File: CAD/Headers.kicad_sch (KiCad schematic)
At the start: 58 parts, among them J1 SWD, J10 OUT_0, J11 OUT_1, J12 OUT_2, J13 TEMP_0, J14 TEMP_1, J15 TEMP_2, J16 EXPANSION, J17 ESP_DB, J18 250-502/000-006, J19 A2543WV-5P, J2 A2543WV-2P, J20 IO_1, J21 IO_2, J22 A2543WV-2P, J23 CAN_1_OUT, J24 DRIVER_2, J25 DRIVER_1, J26 DRIVER_0, J28 SPI_DB, J3 OUT_6, J31 IO_3, J33 A2543WV-4P, J34 A2543WV-4P, J35 DRIVER_3, J36 DRIVER_4, J37 DRIVER_5, J38 CAN_0_OUT, J39 PANELDUE_SD, J4 OUT_7, J41 TEMP_3, J42 DS_LED, J44 IO_7_ISO_OUT, J47 IO_8_ISO_OUT, J48 SBC, J5 OUT_8, J50 EXT_5V_IN, J51 IO_4, J53 IO_5, J54 IO_6, J55 IO_7, J56 IO_8, J59 A2543WV-2P, J6 OUT_3, J60 A2543WV-2P, J61 IO_7_ISO_IN, J62 IO_8_ISO_IN, J7 OUT_4, J8 OUT_5

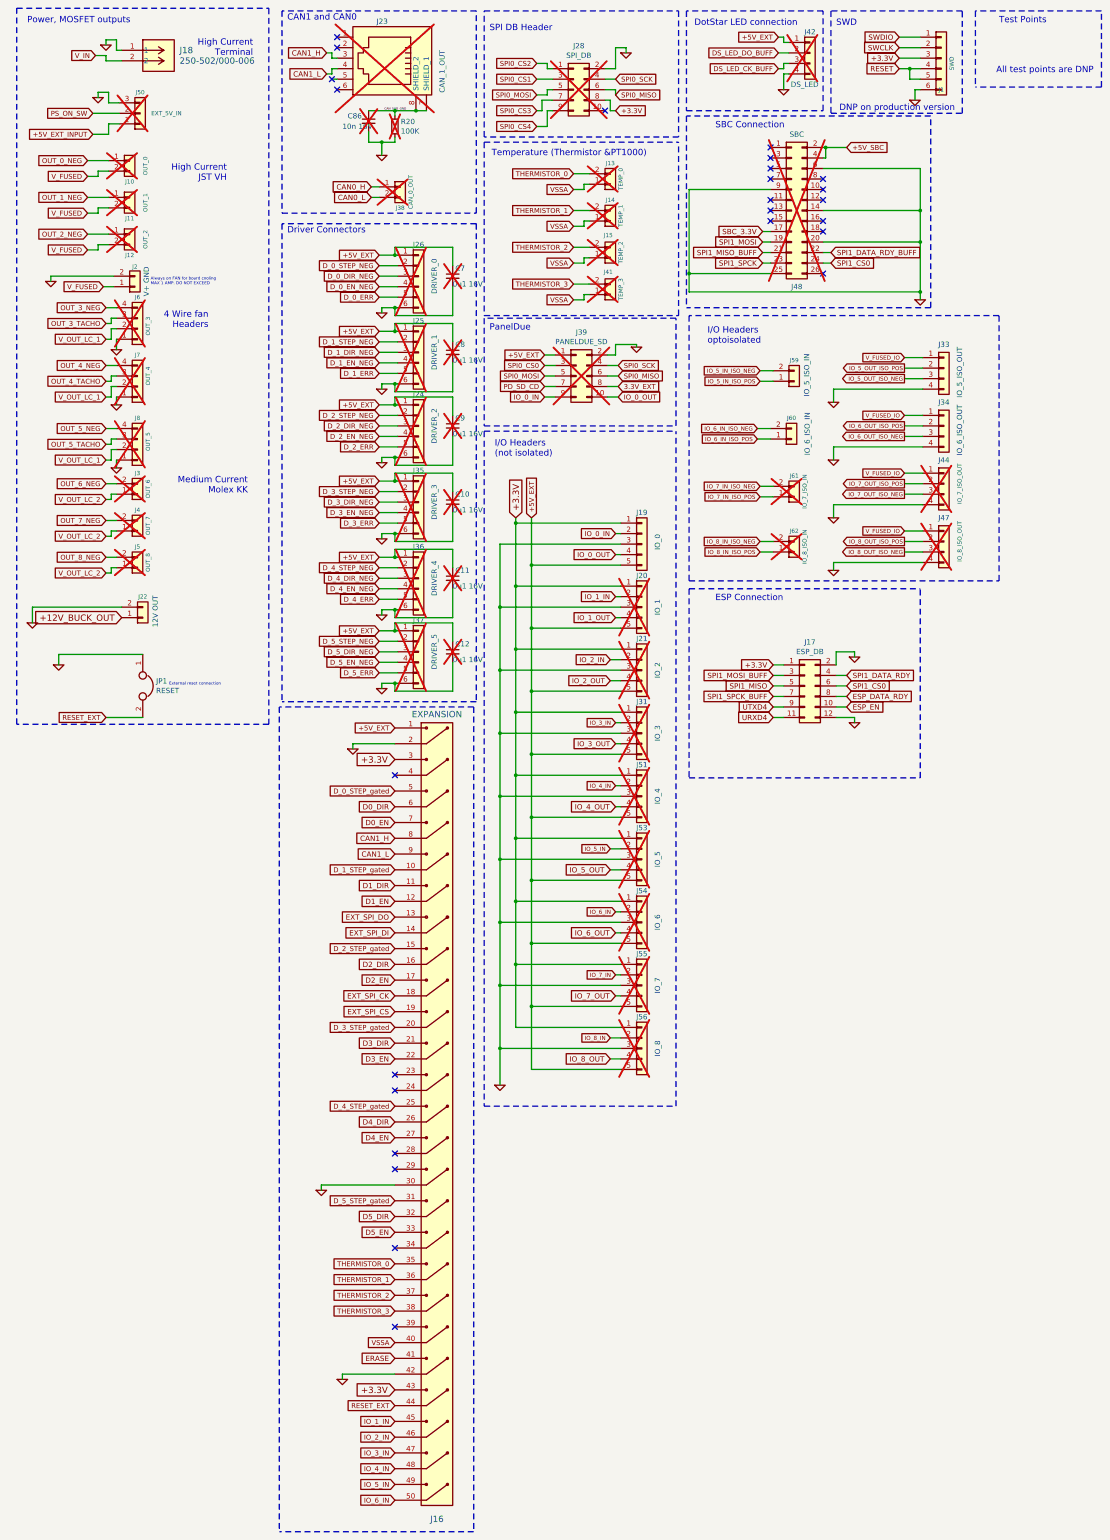
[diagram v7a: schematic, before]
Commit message: Remove Connectors
Removed all old and unused connectors outright from the schematic
Added several other connectors to DNP and Exclude BOM for production since those connectors have never been used.
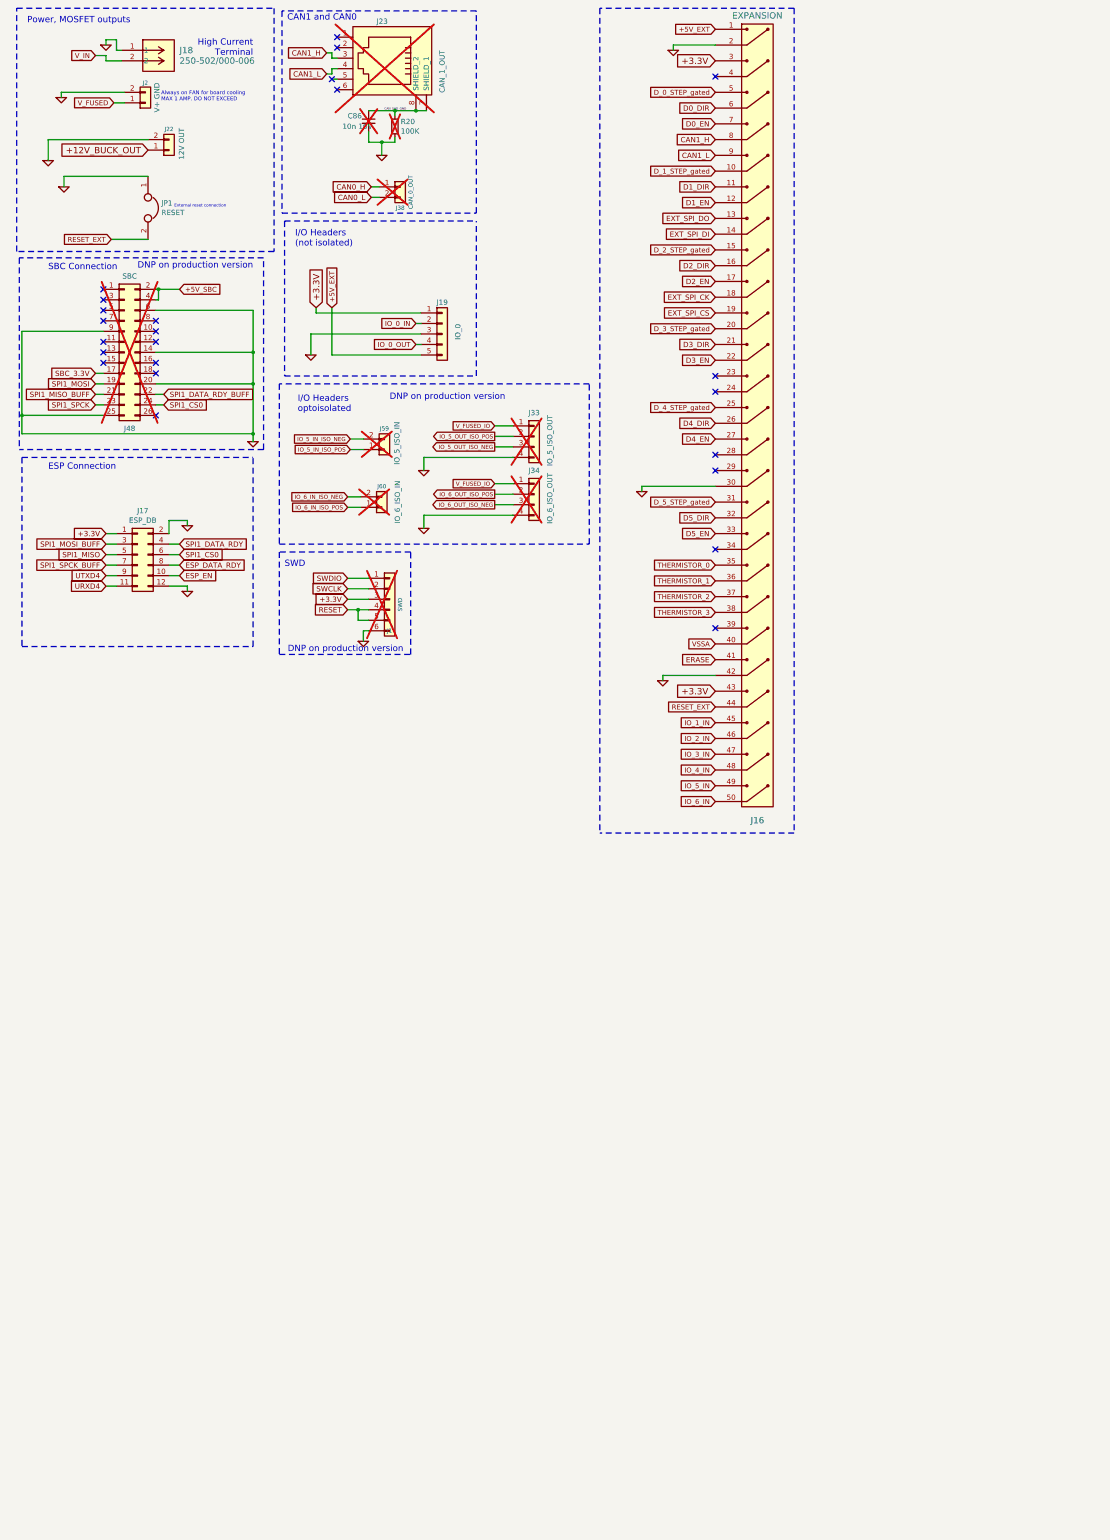
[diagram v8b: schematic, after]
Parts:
- removed C10, C11, C12, C7, C8, C9: 0u1 16V, Capacitor_SMD:C_0402_1005Metric_Wbry, symbol Device:C_Small
- removed J10: OUT_0, Connector_JST:JST_VH_B2P-VH-B_1x02_P3.96mm_Vertical, symbol Connector_Generic:Conn_01x02
- removed J11: OUT_1, Connector_JST:JST_VH_B2P-VH-B_1x02_P3.96mm_Vertical, symbol Connector_Generic:Conn_01x02
- removed J12: OUT_2, Connector_JST:JST_VH_B2P-VH-B_1x02_P3.96mm_Vertical, symbol Connector_Generic:Conn_01x02
- removed J13: TEMP_0, Connector_Molex:Wurth_61900211121-1x02_P2.54mm_Vertical-(Molex_KK-254_AE-6410-02Acompatible), symbol Connector_Generic:Conn_01x02
- removed J14: TEMP_1, Connector_Molex:Wurth_61900211121-1x02_P2.54mm_Vertical-(Molex_KK-254_AE-6410-02Acompatible), symbol Connector_Generic:Conn_01x02
- removed J15: TEMP_2, Connector_Molex:Wurth_61900211121-1x02_P2.54mm_Vertical-(Molex_KK-254_AE-6410-02Acompatible), symbol Connector_Generic:Conn_01x02
- removed J20: IO_1, Connector_Molex:Wurth_61900511121-1x05_P2.54mm_Vertical(Molex_KK-254_AE-6410-05A_Compatibe), symbol Connector_Generic:Conn_01x05
- removed J21: IO_2, Connector_Molex:Wurth_61900511121-1x05_P2.54mm_Vertical(Molex_KK-254_AE-6410-05A_Compatibe), symbol Connector_Generic:Conn_01x05
- removed J24: DRIVER_2, Connector_Molex:Wurth_61900611121-1x06_P2.54mm_Vertical(Molex_KK-254_AE-6410-06A_Compatibe), symbol Connector_Generic:Conn_01x06
- removed J25: DRIVER_1, Connector_Molex:Wurth_61900611121-1x06_P2.54mm_Vertical(Molex_KK-254_AE-6410-06A_Compatibe), symbol Connector_Generic:Conn_01x06
- removed J26: DRIVER_0, Connector_Molex:Wurth_61900611121-1x06_P2.54mm_Vertical(Molex_KK-254_AE-6410-06A_Compatibe), symbol Connector_Generic:Conn_01x06
- removed J28: SPI_DB, complib:MAX_TEMP_DB, symbol Connector_Generic:Conn_02x05_Odd_Even
- removed J3: OUT_6, Connector_Molex:Wurth_61900211121-1x02_P2.54mm_Vertical-(Molex_KK-254_AE-6410-02Acompatible), symbol Connector_Generic:Conn_01x02
- removed J31: IO_3, Connector_Molex:Wurth_61900511121-1x05_P2.54mm_Vertical(Molex_KK-254_AE-6410-05A_Compatibe), symbol Connector_Generic:Conn_01x05
- removed J35: DRIVER_3, Connector_Molex:Wurth_61900611121-1x06_P2.54mm_Vertical(Molex_KK-254_AE-6410-06A_Compatibe), symbol Connector_Generic:Conn_01x06
- removed J36: DRIVER_4, Connector_Molex:Wurth_61900611121-1x06_P2.54mm_Vertical(Molex_KK-254_AE-6410-06A_Compatibe), symbol Connector_Generic:Conn_01x06
- removed J37: DRIVER_5, Connector_Molex:Wurth_61900611121-1x06_P2.54mm_Vertical(Molex_KK-254_AE-6410-06A_Compatibe), symbol Connector_Generic:Conn_01x06
- removed J39: PANELDUE_SD, Connector_IDC:IDC-Header_2x05_P2.54mm_Vertical, symbol Connector_Generic:Conn_02x05_Odd_Even
- removed J4: OUT_7, Connector_Molex:Wurth_61900211121-1x02_P2.54mm_Vertical-(Molex_KK-254_AE-6410-02Acompatible), symbol Connector_Generic:Conn_01x02
- removed J41: TEMP_3, Connector_Molex:Wurth_61900211121-1x02_P2.54mm_Vertical-(Molex_KK-254_AE-6410-02Acompatible), symbol Connector_Generic:Conn_01x02
- removed J42: DS_LED, Connector_Molex:Wurth_61900411121-1x04_P2.54mm_Vertical(Molex_KK-254_AE-6410-04A_Compatible), symbol Connector_Generic:Conn_01x04
- removed J44: IO_7_ISO_OUT, Connector_Molex:Wurth_61900411121-1x04_P2.54mm_Vertical(Molex_KK-254_AE-6410-04A_Compatible), symbol Connector_Generic:Conn_01x04
- removed J47: IO_8_ISO_OUT, Connector_Molex:Wurth_61900411121-1x04_P2.54mm_Vertical(Molex_KK-254_AE-6410-04A_Compatible), symbol Connector_Generic:Conn_01x04
- removed J5: OUT_8, Connector_Molex:Wurth_61900211121-1x02_P2.54mm_Vertical-(Molex_KK-254_AE-6410-02Acompatible), symbol Connector_Generic:Conn_01x02
- removed J50: EXT_5V_IN, Connector_Molex:Wurth_61900311121-1x03_P2.54mm_Vertical(Molex_KK-254_AE-6410-03A_Compatible), symbol Connector_Generic:Conn_01x03
- removed J51: IO_4, Connector_Molex:Wurth_61900511121-1x05_P2.54mm_Vertical(Molex_KK-254_AE-6410-05A_Compatibe), symbol Connector_Generic:Conn_01x05
- removed J53: IO_5, Connector_Molex:Wurth_61900511121-1x05_P2.54mm_Vertical(Molex_KK-254_AE-6410-05A_Compatibe), symbol Connector_Generic:Conn_01x05
- removed J54: IO_6, Connector_Molex:Wurth_61900511121-1x05_P2.54mm_Vertical(Molex_KK-254_AE-6410-05A_Compatibe), symbol Connector_Generic:Conn_01x05
- removed J55: IO_7, Connector_Molex:Wurth_61900511121-1x05_P2.54mm_Vertical(Molex_KK-254_AE-6410-05A_Compatibe), symbol Connector_Generic:Conn_01x05
- removed J56: IO_8, Connector_Molex:Wurth_61900511121-1x05_P2.54mm_Vertical(Molex_KK-254_AE-6410-05A_Compatibe), symbol Connector_Generic:Conn_01x05
- removed J6: OUT_3, Connector_Molex:Wurth_61900411121-1x04_P2.54mm_Vertical(Molex_KK-254_AE-6410-04A_Compatible), symbol Connector_Generic:Conn_01x04
- removed J61: IO_7_ISO_IN, Connector_Molex:Wurth_61900211121-1x02_P2.54mm_Vertical-(Molex_KK-254_AE-6410-02Acompatible), symbol Connector_Generic:Conn_01x02
- removed J62: IO_8_ISO_IN, Connector_Molex:Wurth_61900211121-1x02_P2.54mm_Vertical-(Molex_KK-254_AE-6410-02Acompatible), symbol Connector_Generic:Conn_01x02
- removed J7: OUT_4, Connector_Molex:Wurth_61900411121-1x04_P2.54mm_Vertical(Molex_KK-254_AE-6410-04A_Compatible), symbol Connector_Generic:Conn_01x04
- removed J8: OUT_5, Connector_Molex:Wurth_61900411121-1x04_P2.54mm_Vertical(Molex_KK-254_AE-6410-04A_Compatible), symbol Connector_Generic:Conn_01x04
- J1, J33, J34, J59, J60: now not fitted; now left out of the parts list
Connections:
- no-connect marks 25 -> 24
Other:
- note removed: "4 Wire fan Headers"
- note removed: "All test points are DNP"
- note removed: "DotStar LED connection"
- note removed: "Driver Connectors"
- note removed: "High Current JST VH"
- note removed: "Medium Current Molex KK"
- note removed: "PanelDue"
- note removed: "SPI DB Header"
- note removed: "Temperature (Thermistor &PT1000)"
- note removed: "Test Points"
- moved on the sheet: J16, J17, J19, J2, J22, J48, JP1
